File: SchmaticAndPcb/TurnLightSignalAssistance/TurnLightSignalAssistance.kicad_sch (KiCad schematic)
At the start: 25 parts, among them J1 SSD1306_LCD, J2 MPU6050, SW1 Miniature_Toggle_Switch, SW2 SW_DIP_x01, SW3 RelayCyclic, U1 Relay2Channel, U2 PC817-Opto4Channel

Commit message: Fix the schematic
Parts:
- removed R10, R11: 4k7, Resistor_THT:R_Axial_DIN0922_L20.0mm_D9.0mm_P30.48mm_Horizontal, symbol Device:R
- removed R7, R8, R9: 10k, Resistor_THT:R_Axial_DIN0922_L20.0mm_D9.0mm_P30.48mm_Horizontal, symbol Device:R
- added D?: LED, LED_THT:LED_D3.0mm, symbol Device:LED
- added R?: 220, Resistor_THT:R_Axial_DIN0922_L20.0mm_D9.0mm_P30.48mm_Horizontal, symbol Device:R
- added U3: Module-LM2596, symbol New_Library:Module-LM2596
- R1, R2, R3, R4, R5, R6: value 220 -> 1K
- SW1: value Miniature_Toggle_Switch -> TurnSignalSwitch
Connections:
- net RelayLeft is gone; now on net RSignalRight: U1.8 (NO1)
- net RelayRight is gone; now on net RSignalLeft: U1.5 (NO2)
- net BlinkLeft: now also U1.7 (NC2); no longer U1.6 (COM2)
- net BlinkRight: now also U1.10 (NC1); no longer U1.9 (COM1)
- net GND: now also U2.14 (G), U2.16 (G), U2.6 (G), U2.8 (G), D?.1 (K), U3.4 (Out_DC+); no longer SW3.4 (Common)
- net RSignalLeft: now also U2.3 (IN2); no longer U1.10 (NC1)
- net RSignalRight: now also U2.1 (IN1); no longer U1.7 (NC2)
- net SignalLeft: now also U2.11 (U2)
- net SignalRight: now also U2.9 (U1)
- net at SW1.1 (Left): now also U1.6 (COM2); no longer U1.2 (IN1)
- net at SW1.3 (Right): now also U1.9 (COM1); no longer U1.1 (IN2)
- net EnableFunction: no longer names the net of SW2.2
- net EnableFunction: now also U3.1 (IN_DC+); no longer A1.12 (D9)
- net VCC renamed +5V
- net +5V: now also U3.3 (OUT_DC+); no longer SW1.2, SW2.1
- new net: D?.2 (A), R?.1
- new net +BATT: SW1.2, SW2.1
- new net -BATT: SW3.4 (Common), U3.2 (IN_DC-)
- new net AliveLed: A1.12 (D9), R?.2
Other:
- note added: "Alive LED"
- note added: "Convert control signal"
- note added: "Cyclic toggling GND"
- note added: "Led right left"
- note added: "MPU6050"
- note added: "OLED"
- note added: "Power source"
- note added: "Turn signal select"
- company: (none) -> Bosch VN
- title: (none) -> Turn light signal assistance
- moved on the sheet: J1, J2, U1

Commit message: fixing and optimizing schematic
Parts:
- removed SW1: TurnSignalSwitch, symbol New_Library:Miniature_Toggle_Switch
- removed SW2: SW_DIP_x01, symbol Switch:SW_DIP_x01
- removed U1: Relay2Channel, symbol New_Library:Relay2Channel
- removed U2: PC817-Opto4Channel, symbol New_Library:PC817-Opto4Channel
- added D7, D8: DIODE, symbol pspice:DIODE
- added Q1: 2SC1815, Package_TO_SOT_THT:TO-92_Inline, symbol Transistor_BJT:2SC1815
- added R1, R10, R2, R9: 1K, Resistor_THT:R_Axial_DIN0309_L9.0mm_D3.2mm_P12.70mm_Horizontal, symbol Device:R
- added R11: 10K, Resistor_THT:R_Axial_DIN0309_L9.0mm_D3.2mm_P12.70mm_Horizontal, symbol Device:R
- added SW1: SW_DIP_x01, symbol Switch:SW_DIP_x01
- added U1: TurnSwitch, symbol New_Library:MinatureSwitch
- added U2, U3: PC817, Package_DIP:DIP-4_W7.62mm, symbol Isolator:PC817
- added U4: Relay1Channel, symbol New_Library:Relay1Channel
- R12: renamed from R?; footprint Resistor_THT:R_Axial_DIN0922_L20.0mm_D9.0mm_P30.48mm_Horizontal -> Resistor_THT:R_Axial_DIN0309_L9.0mm_D3.2mm_P12.70mm_Horizontal
- R4: renamed from R3; footprint (none) -> Resistor_THT:R_Axial_DIN0309_L9.0mm_D3.2mm_P12.70mm_Horizontal
- R5: footprint Resistor_THT:R_Axial_DIN0922_L20.0mm_D9.0mm_P30.48mm_Horizontal -> Resistor_THT:R_Axial_DIN0309_L9.0mm_D3.2mm_P12.70mm_Horizontal
- R6: renamed from R2; footprint Resistor_THT:R_Axial_DIN0922_L20.0mm_D9.0mm_P30.48mm_Horizontal -> Resistor_THT:R_Axial_DIN0309_L9.0mm_D3.2mm_P12.70mm_Horizontal
- R7: renamed from R4; footprint Resistor_THT:R_Axial_DIN0922_L20.0mm_D9.0mm_P30.48mm_Horizontal -> Resistor_THT:R_Axial_DIN0309_L9.0mm_D3.2mm_P12.70mm_Horizontal
- R8: renamed from R6; footprint Resistor_THT:R_Axial_DIN0922_L20.0mm_D9.0mm_P30.48mm_Horizontal -> Resistor_THT:R_Axial_DIN0309_L9.0mm_D3.2mm_P12.70mm_Horizontal
- gave numbers to parts that had none: 1
- renumbered D3 to D2, D5 to D3, D2 to D4, D4 to D5, R1 to R3, SW3 to SW2, U3 to U5
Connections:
- net +5V: now also R10.2, R9.2, SW1.1, U4.1 (DC+); no longer A1.30 (VIN)
- net +BATT: now also U5.1 (IN_DC+), U1.2 (Com)
- net -BATT: now also U2.2, U3.2
- net BlinkLeft: now also D7.1 (K), R2.2, U1.3 (Out2); no longer A1.14 (D11)
- net BlinkRight: now also D8.1 (K), R1.2, U1.1 (Out1); no longer A1.13 (D10)
- net GND: now also Q1.1 (E), U2.3, U3.3, U4.2 (DC-); no longer SW2.2 (GND)
- net LedBlinkGnd: now also U4.5 (COM)
- net SignalLeft: now also A1.14 (D11), R10.1, U3.4; no longer A1.16 (D13)
- net SignalRight: now also A1.13 (D10), R9.1, U2.4; no longer A1.15 (D12)
- net at A1.27 (+5V): now also SW1.2
- new net: R2.1, U3.1
- new net: Q1.2 (C), SW2.2 (GND)
- new net: D7.2 (A), D8.2 (A), R11.2
- new net: Q1.3 (B), R11.1
- new net: R1.1, U2.1
- new net LightControl: A1.15 (D12), U4.3 (Control)
- new net RelayOutGND: U4.4 (NC)
- no-connect marks 18 -> 16
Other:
- note added: "Arduino Nano - Main"
- note added: "Isolate control signal"
- note added: "Relay control GND"
- note removed: "Convert control signal"
- moved on the sheet: A1, D9, J1, R12, SW2, U5

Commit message: update document and fix schematic
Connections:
- net LedBlinkGnd: no longer SW2.3 (NO)
- net RelayOutGND: now also SW2.3 (NO)
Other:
- note added: "OLED (Optional. Just for monitor when demo)"
- note removed: "OLED"
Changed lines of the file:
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@@
     (effects (font (size 1.27 1.27)) (justify left bottom))
   )
-  (text "OLED" (at 233.68 95.25 0)
+  (text "OLED (Optional. Just for monitor when demo)" (at 233.68 95.25 0)
     (effects (font (size 1.27 1.27)) (justify left bottom))
   )
@@
   )
   (label "LedBlinkGnd" (at 31.75 85.09 90)
+    (effects (font (size 1.27 1.27)) (justify left bottom))
+  )
+  (label "RelayOutGND" (at 204.47 106.68 0)
     (effects (font (size 1.27 1.27)) (justify left bottom))
   )
@@
     (effects (font (size 1.27 1.27)) (justify left bottom))
   )
-  (label "LedBlinkGnd" (at 203.2 106.68 0)
-    (effects (font (size 1.27 1.27)) (justify left bottom))
-  )

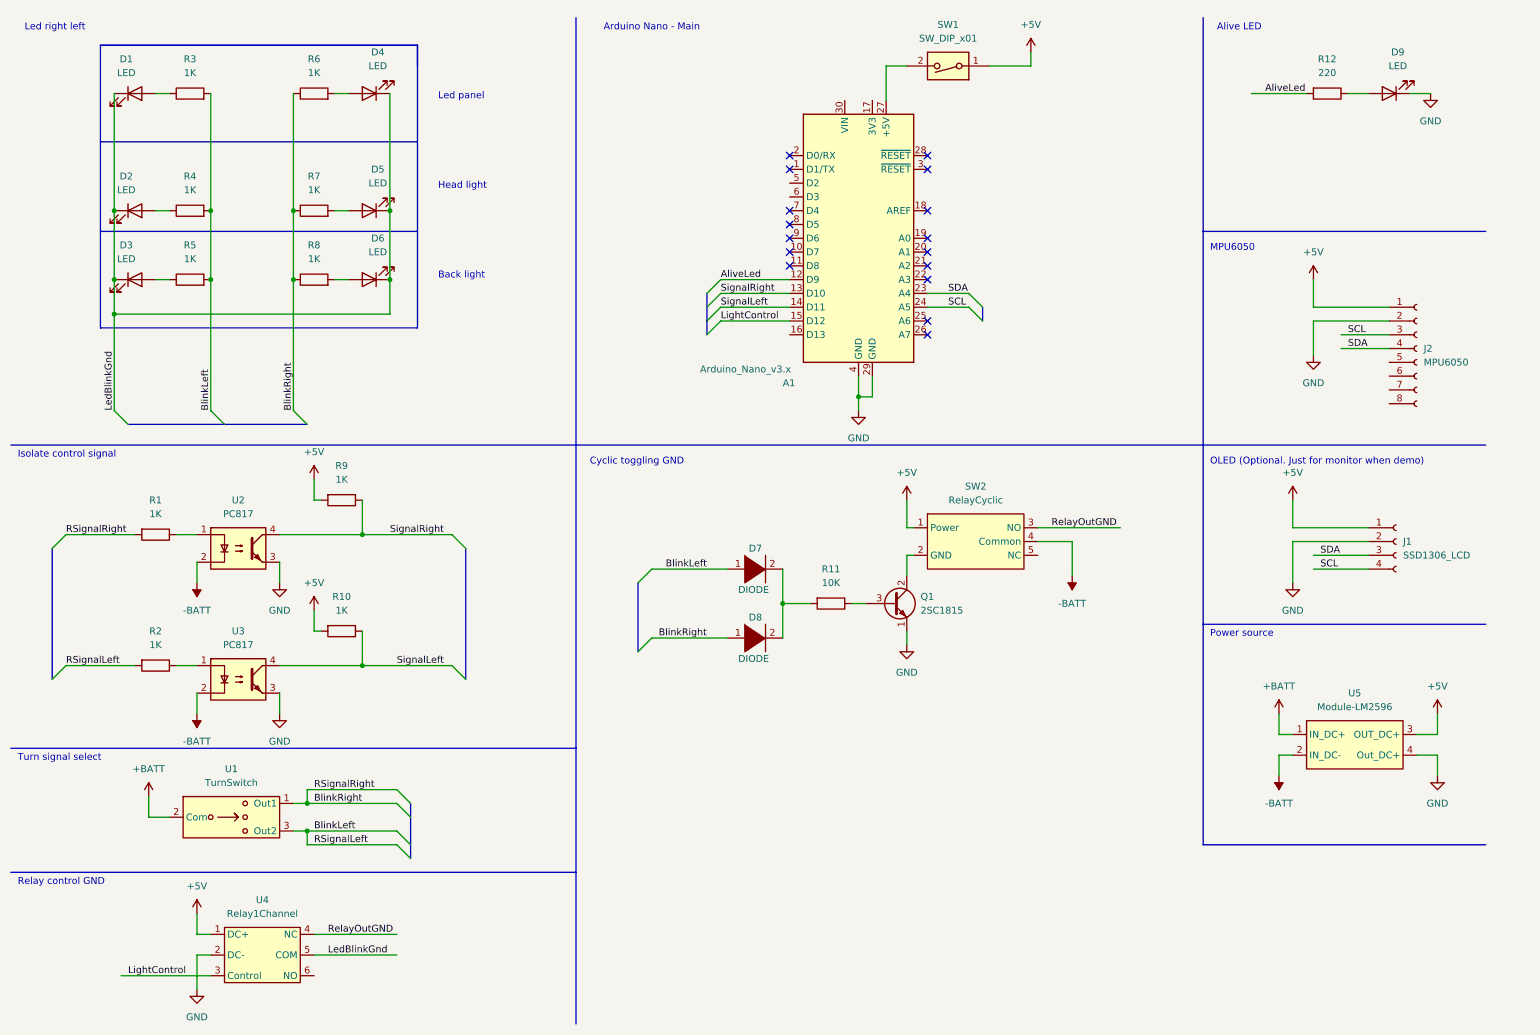
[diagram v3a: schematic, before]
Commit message: Separate the simulate part and main part. Update the document
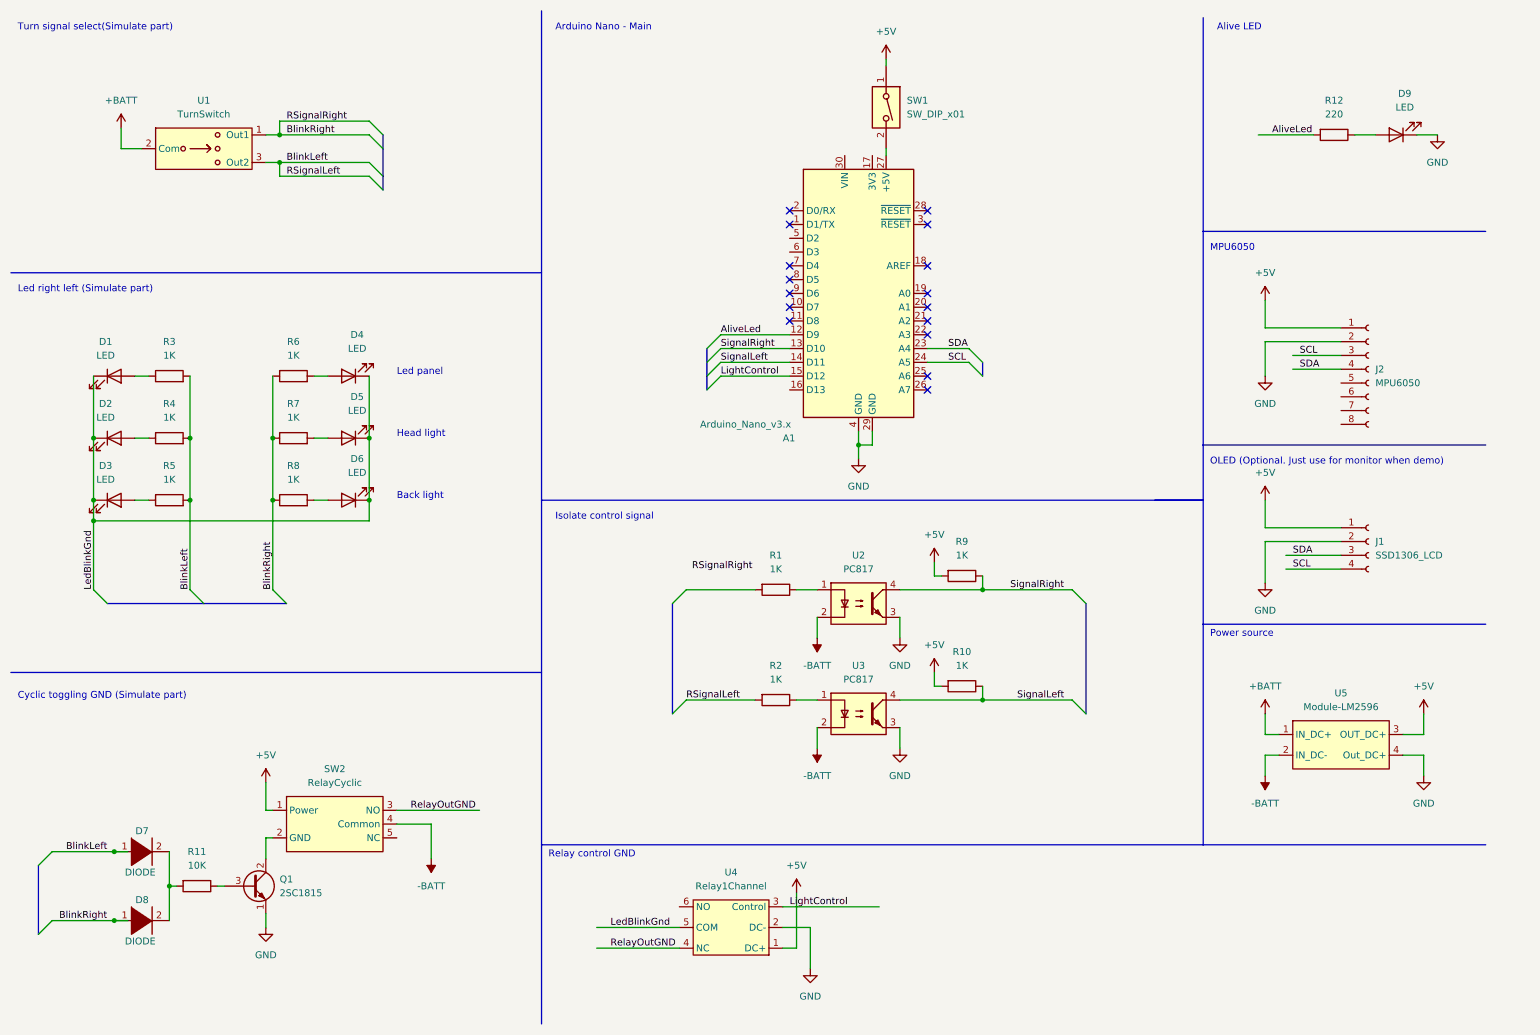
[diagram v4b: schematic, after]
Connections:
- net BlinkRight: no longer R1.2
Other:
- note added: "Cyclic toggling GND (Simulate part)"
- note added: "Led right left (Simulate part)"
- note added: "OLED (Optional. Just use for monitor when demo)"
- note added: "Turn signal select(Simulate part)"
- note removed: "Cyclic toggling GND"
- note removed: "Led right left"
- note removed: "OLED (Optional. Just for monitor when demo)"
- note removed: "Turn signal select"
- moved on the sheet: A1, D1, D2, D3, D4, D5, D6, D7, D8, D9, J1, J2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
